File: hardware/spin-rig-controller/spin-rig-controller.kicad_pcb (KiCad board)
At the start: 4 copper layers, 110 x 80 mm, 170 parts, among them J101 PACK IN, J102 BRAKE RES, J103 DRIVER, J104 5V AUX, J201 USB4110GFA, J202 PI, J203 QWIIC, J301 CL57T CONTROL, J302 ENCODER, J303 INDEX, J304 GNSS, Q101 NCE60P50K, Q102 AO4264E, SW201 BOOT, SW202 RESET, U101 INA238AIDGSR, U102 TLV3011AIDBVR, U103 UCC27517DBVR, U104 TPS54560BDDAR, U105 AP2112K-3.3TRG1, U201 ESP32-S3FN8, U301 SN74ACT244PWR, U302 AM26LV32EIDR, U303 SN74LVC1G17DBVR, U304 SN74LVC2G125DCTR, Y201 40 MHz

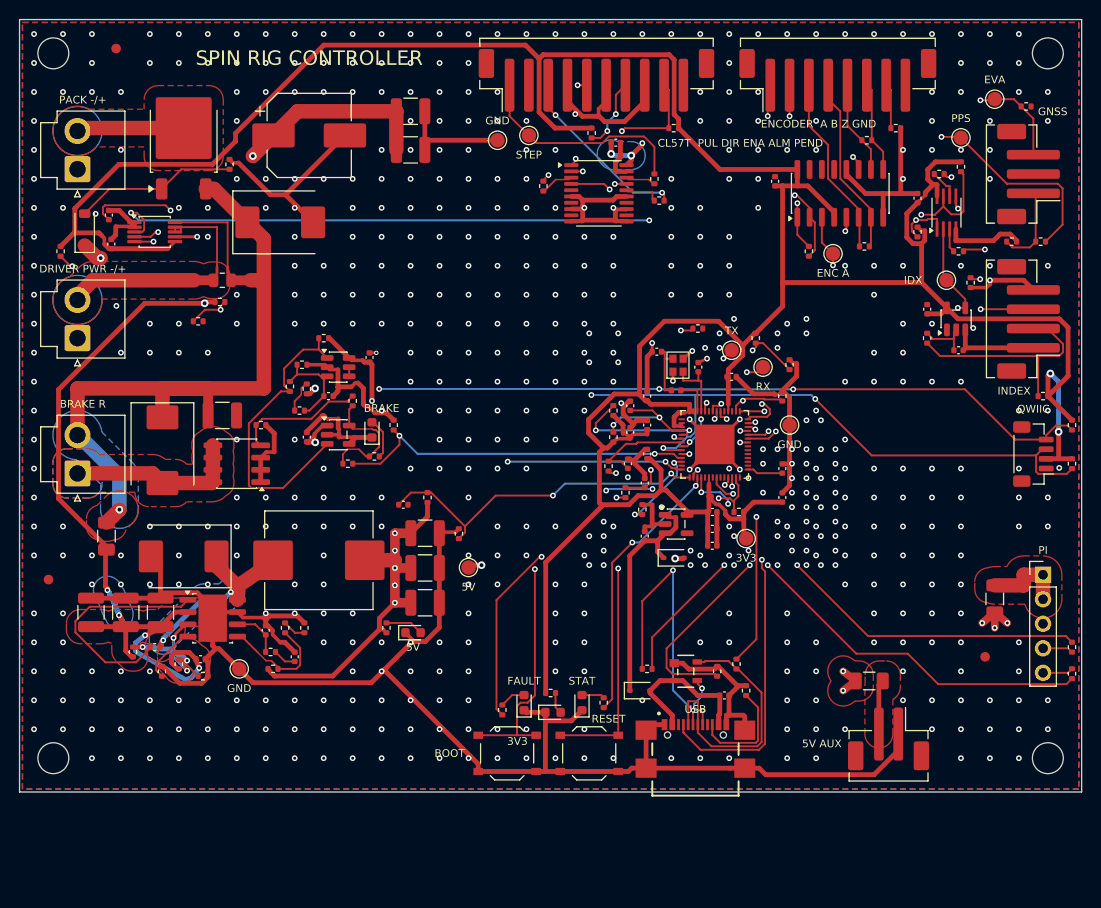
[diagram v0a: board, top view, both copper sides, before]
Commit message: hardware(spin-rig-controller): the driver's own plugs -- XT60 pack input, CL57T 3.5 mm headers in its pin order, and an encoder pass-through
After the first review, the connectors change so the assembly plugs together instead of being wired up:
- J101 is an XT60PW-M (right angle, top edge), matching the rig's pack and anti-spark switch;
- J103 (driver feed), J301 (control) and the new J305 (encoder out) are 3.5 mm Phoenix MC headers that take
  the CL57T's own pluggable plugs, in its order: P4 +VDC GND; P1 PUL+ PUL- DIR+ DIR- ENA+ ENA- ALM BRK COM-;
  P2 EB+ EB- EA+ EA- VCC EGND. The silkscreen names every pin;
- the motor's encoder extension lead lands on J302 (right edge) and passes through to J305; the AM26LV32E
  reads A and B on the way. J302 is numbered from the bottom so the six traces nest around the corner;
- J303, J304 and J104 become through-hole JST PH. J102 (brake resistor) is now the only VH connector, which
  ends the three look-alike power connectors.

The CL57T V4.x has no in-position output: its ALM and BRK are open-collector to a shared COM- (CL57T V4.0
manual, CL42T/CL86T V4.1 manuals). The input that read PEND now reads BRK (DRV_BRK, GPIO2), and ENC_Z is
dropped (the encoder has no index; GPIO35 is free). The Qwiic connector moves beside the INA238.

Through-hole parts (design.HAND) are out of the JLC BOM and CPL; make_fab.py lists them in -hand.csv
(29 extended part types now, about $23 of JLC parts a board). The router's leftovers are closed by
gen/hand_fixes.py, planned against the copper around each (gen/region.py lists a window's copper).
ERC 0 errors (the shared SP0503 symbol's 4 warnings); DRC 0 errors, 0 unconnected, schematic parity clean;
tools/check_board_parity.py passes. Still to measure: the CL57T's terminal pitch (3.5 mm assumed). Not ordered.

Co-Authored-By: Claude Opus 5.5 <noreply@anthropic.com>
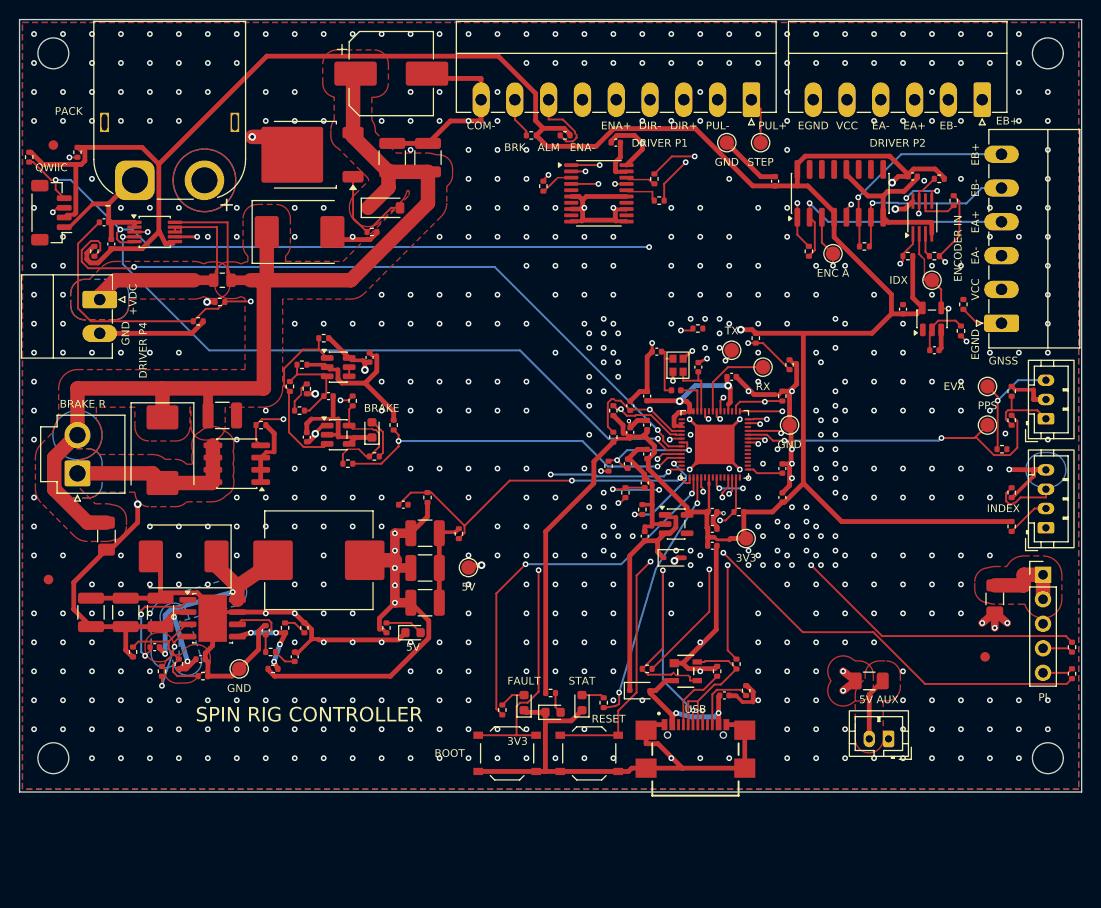
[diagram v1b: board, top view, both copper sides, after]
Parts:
- removed R315: 120, Resistor_SMD:R_0402_1005Metric
- added J305: ENCODER OUT, Connector_Phoenix_MC:PhoenixContact_MC_1,5_6-G-3.5_1x06_P3.50mm_Horizontal, F.Cu at (199.7, 108.3)
- J101: footprint Connector_JST:JST_VH_B2P-VH_1x02_P3.96mm_Vertical -> Connector_AMASS:AMASS_XT60PW-M_1x02_P7.20mm_Horizontal
- J103: value DRIVER -> DRIVER PWR; footprint Connector_JST:JST_VH_B2P-VH_1x02_P3.96mm_Vertical -> Connector_Phoenix_MC:PhoenixContact_MC_1,5_2-G-3.5_1x02_P3.50mm_Horizontal
- J104: footprint Connector_JST:JST_PH_B2B-PH-SM4-TB_1x02-1MP_P2.00mm_Vertical -> Connector_JST:JST_PH_B2B-PH-K_1x02_P2.00mm_Vertical
- J301: footprint Connector_JST:JST_PH_B10B-PH-SM4-TB_1x10-1MP_P2.00mm_Vertical -> Connector_Phoenix_MC:PhoenixContact_MC_1,5_9-G-3.5_1x09_P3.50mm_Horizontal
- J302: value ENCODER -> ENCODER IN; footprint Connector_JST:JST_PH_B8B-PH-SM4-TB_1x08-1MP_P2.00mm_Vertical -> Connector_Phoenix_MC:PhoenixContact_MC_1,5_6-G-3.5_1x06_P3.50mm_Horizontal
- J303: footprint Connector_JST:JST_PH_B4B-PH-SM4-TB_1x04-1MP_P2.00mm_Vertical -> Connector_JST:JST_PH_B4B-PH-K_1x04_P2.00mm_Vertical
- J304: footprint Connector_JST:JST_PH_B3B-PH-SM4-TB_1x03-1MP_P2.00mm_Vertical -> Connector_JST:JST_PH_B3B-PH-K_1x03_P2.00mm_Vertical
- moved R214 111.5 mm to (101.0, 114.2)
- moved R213 107.9 mm to (106.0, 113.8)
- moved J203 104.7 mm to (103.3, 120.0)
- moved R326 35.6 mm to (201.8, 144.5)
- moved D101 31.1 mm to (137.8, 119.5), turned to 0 degrees
- moved J302 30.3 mm to (201.7, 131.4), turned to 90 degrees
- moved TP302 29.9 mm to (200.2, 142.0)
- moved TP304 29.8 mm to (200.2, 138.0)
- moved J304 25.4 mm to (206.3, 141.3)
- moved TP301 24.0 mm to (176.8, 112.8)
- moved TP306 23.8 mm to (173.2, 112.8)
- moved R317 22.2 mm to (202.8, 149.0)
- moved J303 21.7 mm to (206.3, 152.6)
- moved R316 19.5 mm to (197.8, 129.5), turned to 90 degrees
- moved R324 18.7 mm to (202.8, 141.5), turned to 90 degrees
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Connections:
- net PEND renamed DRV_BRK
- J103 pad 1: GND -> /Power/VDRV
- J103 pad 2: /Power/VDRV -> GND
- J301 pad 8: GND -> /Driver and timing I/O/BRK_P
- J301 pad 9: /Driver and timing I/O/PEND_P -> GND
- J302 pad 1: /Driver and timing I/O/ENC_A_P -> /Driver and timing I/O/ENC_GND
- J302 pad 2: /Driver and timing I/O/ENC_A_N -> /Driver and timing I/O/ENC_VCC
- J302 pad 3: /Driver and timing I/O/ENC_B_P -> /Driver and timing I/O/ENC_A_N
- J302 pad 4: /Driver and timing I/O/ENC_B_N -> /Driver and timing I/O/ENC_A_P
- J302 pad 5: /Driver and timing I/O/ENC_Z_P -> /Driver and timing I/O/ENC_B_N
- J302 pad 6: /Driver and timing I/O/ENC_Z_N -> /Driver and timing I/O/ENC_B_P
- R311 pad 1: /Driver and timing I/O/PEND_P -> /Driver and timing I/O/BRK_P
- R312 pad 1: /Driver and timing I/O/PEND_P -> /Driver and timing I/O/BRK_P
- U201 pad 40: ENC_Z -> unconnected-(U201-GPIO35-Pad40)
- U302 pad 10: /Driver and timing I/O/ENC_Z_P -> unconnected-(U302-3A-Pad10)
- U302 pad 11: ENC_Z -> unconnected-(U302-3Y-Pad11)
- U302 pad 9: /Driver and timing I/O/ENC_Z_N -> unconnected-(U302-3B-Pad9)
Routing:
- net /Driver and timing I/O/PEND_P: track 47.2 -> 0.00 mm, vias 2 -> 0
- net /Driver and timing I/O/BRK_P: track 0.00 -> 47.1 mm, vias 0 -> 1
- net /MCU/USB_CC1: track 50.8 -> 7.04 mm, vias 2 -> 0
- net I2C_SDA: track 128.8 -> 86.2 mm
- net GND: track 389.6 -> 353.3 mm, vias 569 -> 577
- net ENC_Z: track 35.3 -> 0.00 mm, vias 2 -> 0
- net /Driver and timing I/O/ENC_GND: track 4.65 -> 37.3 mm
- net /Driver and timing I/O/ENC_A_N: track 17.7 -> 50.3 mm, vias 2 -> 1
- net /Power/VMAIN: track 135.2 -> 106.8 mm, vias 3 -> 0
- net /Driver and timing I/O/ENC_VCC: track 0.00 -> 27.5 mm
- net PPS: track 61.2 -> 34.8 mm
- net /Driver and timing I/O/ENC_A_P: track 20.2 -> 44.2 mm, vias 2 -> 1
- net I2C_SCL: track 120.6 -> 98.8 mm, vias 5 -> 4
- net /Power/VMAIN_F: track 95.8 -> 77.2 mm, vias 6 -> 5
- net +3V3: track 348.7 -> 333.6 mm, vias 2 -> 5
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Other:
- board text added: "+VDC"
- board text added: "ALM"
- board text added: "BRK"
- board text added: "COM-"
- board text added: "DIR+"
- board text added: "DIR-"
- board text added: "DRIVER P1"
- board text added: "DRIVER P2"
- board text added: "DRIVER P4"
- board text added: "EA+"
- board text added: "EA-"
- board text added: "EB+"
- board text added: "EB-"
- board text added: "EGND"
- board text added: "ENA+"
- board text added: "ENA-"
- board text added: "ENCODER IN"
- board text added: "PACK"
- board text added: "PUL+"
- board text added: "PUL-"
- board text added: "VCC"
- board text removed: "CL57T PUL DIR ENA ALM PEND"
- board text removed: "DRIVER PWR -/+"
- board text removed: "ENCODER A B Z GND"
- board text removed: "PACK -/+"

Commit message: hardware(spin-rig-controller): ready for a JLC assembly order -- standard-size vias, order-number mark, one origin for gerbers and CPL, and a step-by-step order guide
- The four 0.45 mm vias (the USB D+ pairing and two ground fan-outs) are redrilled from 0.25 to 0.30 mm, JLC's
  standard multilayer via (the Mantis runs 0.40/0.30), so the order carries no small-hole fee. Pads unchanged;
  the board's minimum annular ring rule is now 0.075 mm.
- A "JLCJLCJLCJLC" mark above the title, so the order can put JLC's number there ("Specify a location").
- The PCB title block carries (rev "V1"), where tools/plot_gerbers.sh reads it.
- tools/plot_gerbers.sh gains an opt-in --aux-origin: gerbers and drill from the board's drill/place origin,
  the frame make_fab.py's CPL uses. Without the flag its output is unchanged. README.txt records the frame.
- make_fab.py writes one BOM line per part number (BOOT and RESET shared C318884 on two lines).
- FABRICATION-NOTES.md: the order-notes block updated (vias, annular ring, order number, Economic PCBA,
  preferred tooling-hole spots clear of tracks on every layer), and a step-by-step JLC assembly order guide with
  a pin-1 / polarity table for the placement preview.

DRC 0 errors, 0 unconnected, schematic parity clean; tools/check_board_parity.py passes.

Co-Authored-By: Claude Opus 5.5 <noreply@anthropic.com>
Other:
- board text added: "JLCJLCJLCJLC"
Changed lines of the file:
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@@
 	)
 	(paper "A4")
+	(title_block
+		(rev "V1")
+	)
 	(layers
 		(0 "F.Cu" signal)
@@
 		)
 	)
+	(gr_text "JLCJLCJLCJLC"
+		(at 130 169.28375 0)
+		(layer "F.SilkS")
+		(effects
+			(font
+				(size 1 1)
+				(thickness 0.15)
+			)
+		)
+	)
 	(gr_text "SPIN RIG CONTROLLER ${REVISION}"
 		(at 130 172 0)
@@
 		(at 172.916549 151.136563)
 		(size 0.45)
-		(drill 0.25)
+		(drill 0.3)
 		(layers "F.Cu" "B.Cu")
 		(net "GND")
@@
 		(at 163.113437 141.583451)
 		(size 0.45)
-		(drill 0.25)
+		(drill 0.3)
 		(layers "F.Cu" "B.Cu")
 		(net "GND")
@@
 		(at 170.75 171.55)
 		(size 0.45)
-		(drill 0.25)
+		(drill 0.3)
 		(layers "F.Cu" "B.Cu")
 		(locked yes)
@@
 		(at 169.75 171.55)
 		(size 0.45)
-		(drill 0.25)
+		(drill 0.3)
 		(layers "F.Cu" "B.Cu")
 		(locked yes)

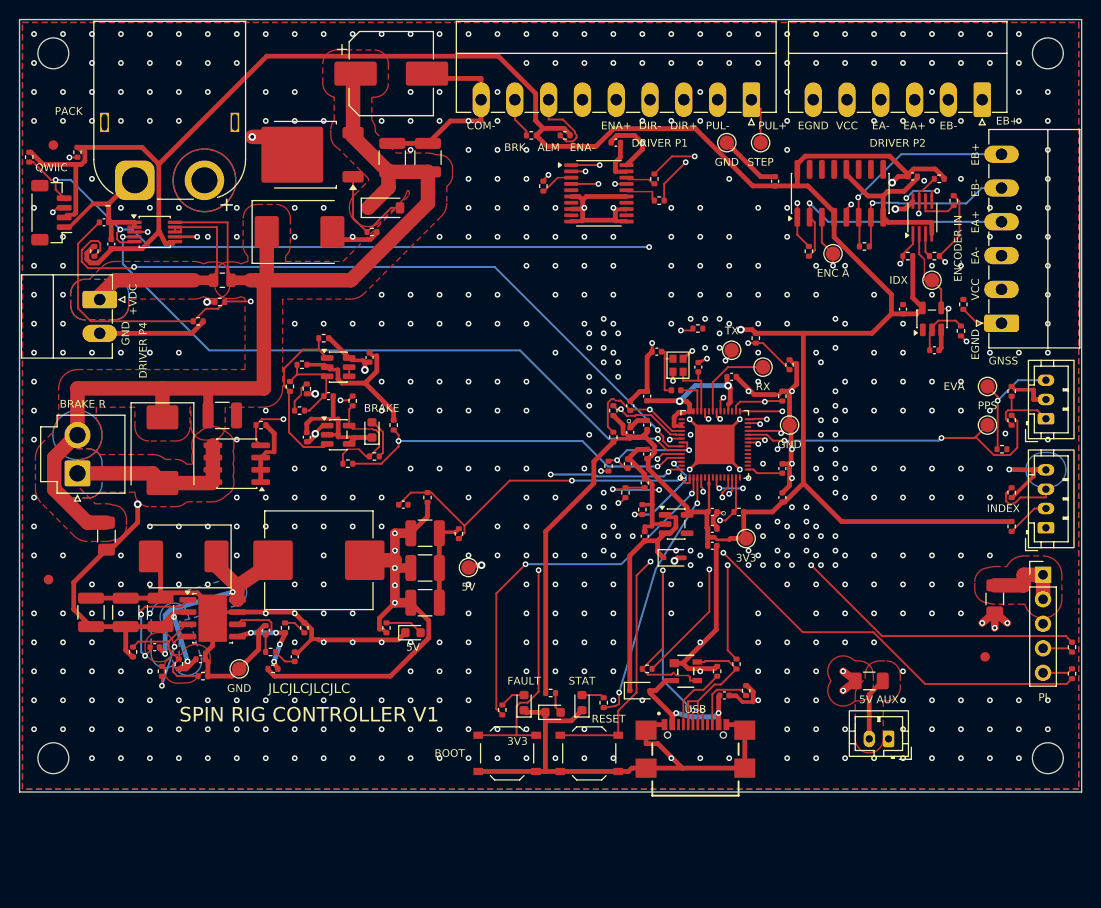
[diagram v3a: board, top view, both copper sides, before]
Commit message: hardware(spin-rig-controller): stacks on the Pi 4B like a HAT -- 2x20 socket on the underside, the Pi's M2.5 holes, USB-C flush
- J202 becomes a 2x20 8.5 mm female socket (Hong Cheng HC-PM254-8.5H-2x20PZ, LCSC C22373925) on the underside,
  on the Pi's header: 5 V in on pins 2 and 4 (F103, 4 A, and a 2 mm feed), the Pi's UART0 on 8 and 10, all
  eight grounds; the Pi's 3.3 V and other GPIOs unconnected. Placed from KiCad's RaspberryPi-HAT template.
- The Pi turns 90 degrees under the left half, its USB/Ethernet end past the bottom edge (the HAT's 65 mm line),
  GPIO edge down x = 56: M2.5 holes H3, H5, H6, H7 on its 58 x 49 mm pattern (H3 was the M3 corner hole),
  M2.5 x 11 mm standoffs. Nothing tall of the Pi's sits under the board; this board's through-hole pins over it
  clear its low parts by about 3 mm.
- J201 (USB-C) moves 0.6 mm in, flush with the edge; the BOOT/RESET switches, their lights and the Qwiic
  connector move to make room.
- Re-placed and re-routed; gen/hand_fixes.py is re-planned for this routing (buck BOOT/EN, C104's ground,
  R101's via, J303's feeder, U101's 3.3 V stub). silk.py puts underside parts' fab text on B.Fab and lets a
  header's end-pin labels step outward.

ERC 0 errors (SP0503's 4 warnings); DRC 0 errors, 0 warnings, 0 unconnected, parity clean; the repo parity gate
passes (173 symbols). README "Stacking on the Pi" covers mounting, clearances, power (no ideal diode: don't
power the Pi from its USB-C while stacked) and the rotor-balance change.

Co-Authored-By: Claude Opus 5.5 <noreply@anthropic.com>
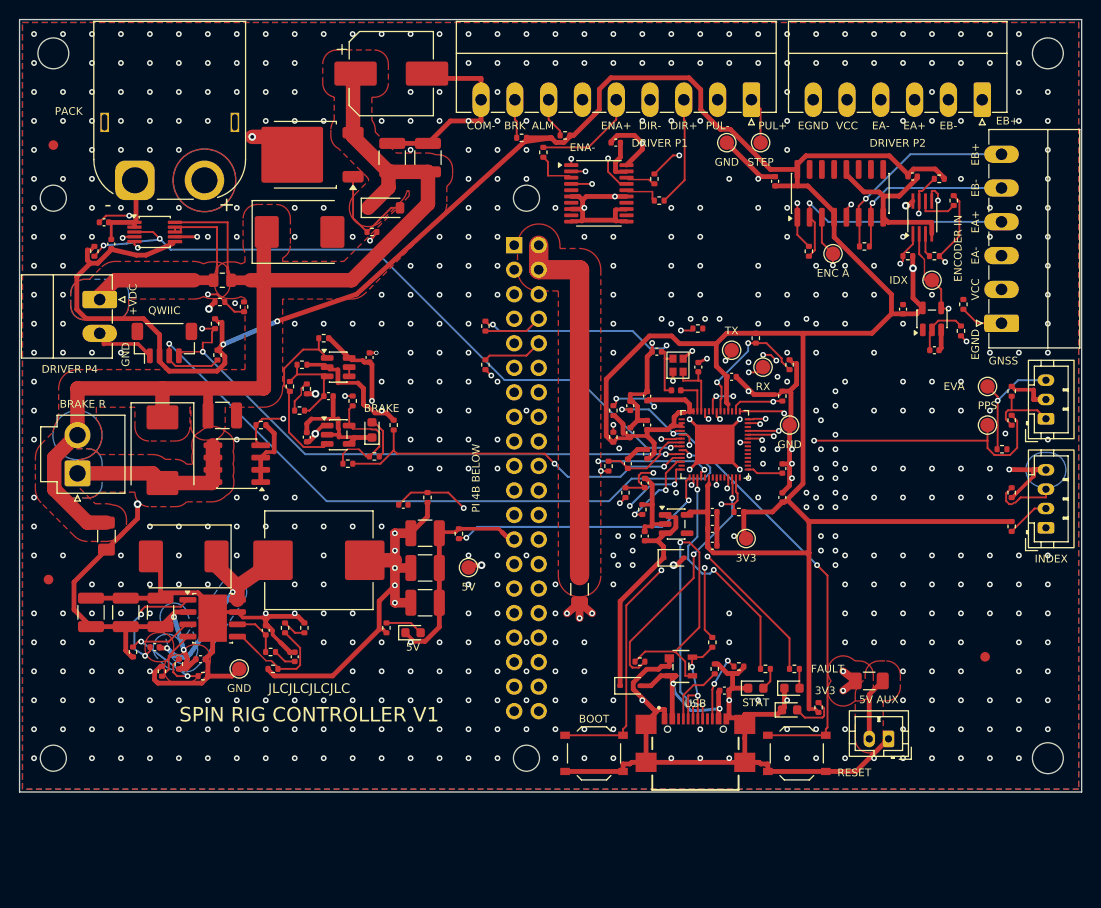
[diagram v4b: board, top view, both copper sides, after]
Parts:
- added H5: M2.5, MountingHole:MountingHole_2.7mm_M2.5, F.Cu at (152.5, 118.5)
- added H6: M2.5, MountingHole:MountingHole_2.7mm_M2.5, F.Cu at (152.5, 176.5)
- added H7: M2.5, MountingHole:MountingHole_2.7mm_M2.5, F.Cu at (103.5, 118.5)
- H3: value M3 -> M2.5; footprint MountingHole:MountingHole_3.2mm_M3 -> MountingHole:MountingHole_2.7mm_M2.5
- J202: value PI -> PI 4B; footprint Connector_PinHeader_2.54mm:PinHeader_1x05_P2.54mm_Vertical -> Connector_PinSocket_2.54mm:PinSocket_2x20_P2.54mm_Vertical; moved to B.Cu
- moved R211 69.3 mm to (148.2, 131.8)
- moved R212 68.7 mm to (148.2, 135.8)
- moved J202 64.5 mm to (151.2, 123.4), turned to 180 degrees
- moved F103 43.0 mm to (158.0, 159.0)
- moved R210 30.5 mm to (180.2, 167.2), turned to 0 degrees
- moved D203 27.8 mm to (180.0, 169.2), turned to 0 degrees
- moved R208 27.8 mm to (182.8, 171.2), turned to 90 degrees
- moved R214 25.8 mm to (120.2, 131.5)
- moved R213 25.5 mm to (120.5, 134.8)
- moved D201 24.5 mm to (179.8, 171.5)
- moved SW202 21.5 mm to (180.5, 176.0)
- moved D202 18.1 mm to (176.2, 169.2), turned to 0 degrees
- moved J203 17.9 mm to (115.0, 133.5), turned to 0 degrees
- moved R209 17.1 mm to (177.2, 167.2), turned to 0 degrees
- moved SW201 9.00 mm to (159.5, 176.0)
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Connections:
- J202 pad 1: +5V_PI -> unconnected-(J202-Pin_1-Pad1)
- J202 pad 3: GND -> unconnected-(J202-Pin_3-Pad3)
- J202 pad 4: /MCU/PI_RX_H -> +5V_PI
- J202 pad 5: /MCU/PI_TX_H -> unconnected-(J202-Pin_5-Pad5)
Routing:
- net +5V_PI: track 8.64 -> 38.5 mm
- net I2C_SCL: track 98.8 -> 73.4 mm
- net /MCU/PI_TX: track 51.0 -> 30.5 mm, vias 2 -> 3
- net /MCU/LED_FAULT: track 39.1 -> 24.1 mm
- net GND: track 353.3 -> 341.4 mm, vias 577 -> 538
- net INA_ALERT: track 81.3 -> 73.6 mm
- net /MCU/PI_RX: track 44.9 -> 37.4 mm
- net +3V3: track 333.6 -> 340.8 mm, vias 5 -> 4
- net +5V: track 160.0 -> 153.8 mm
- net /MCU/USB_DP: track 37.4 -> 43.3 mm
- net ALM: track 15.1 -> 11.1 mm, vias 3 -> 2
- net /Power/BUCK_EN: track 13.2 -> 17.1 mm, vias 0 -> 2
- net /Driver and timing I/O/ALM_P: track 54.3 -> 50.5 mm
- net I2C_SDA: track 86.2 -> 89.7 mm, vias 4 -> 3
- net DRV_OE_N: track 61.7 -> 58.2 mm
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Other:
- board text added: "PI 4B BELOW"
- board text removed: "PI"
